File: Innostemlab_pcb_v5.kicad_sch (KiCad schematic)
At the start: 32 parts, among them J10 I2C, J11 ICSP, J2 USB4105-GF-A-060, J3 BATTERY, J4 MOTOR_1, J5 MOTOR_2, J6 IR1, J7 IR2, J8 IR3, J9 Conn_02x12_Odd_Even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

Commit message: Added caps in TB motor driver, added 22 ohm resistors in usb c data lines, changed part number for AVCC low pass filter, LD1117 datasheet from digikey shows same implementation
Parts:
- added C1, C2: 0.1uf, Capacitor_SMD:C_0805_2012Metric_Pad1.18x1.45mm_HandSolder, symbol Device:C
- added R4, R6: 22, Resistor_SMD:R_0805_2012Metric_Pad1.20x1.40mm_HandSolder, symbol Device:R
- L1: url digikey https://www.digikey.com/en/products/detail/kemet/L0805C100M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 -> https://www.digikey.com/en/products/detail/bourns-inc/MH202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
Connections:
- net +5V: now also C2.2
- net D+: now also R4.1; no longer U5.4 (D+)
- net D-: now also R6.1; no longer U5.3 (D-)
- net GND: now also C1.1, C2.1
- net VBATP_MD: now also C1.2
- new net DNET+: R4.2, U5.4 (D+)
- new net DNET-: R6.2, U5.3 (D-)
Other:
- moved on the sheet: AREF2

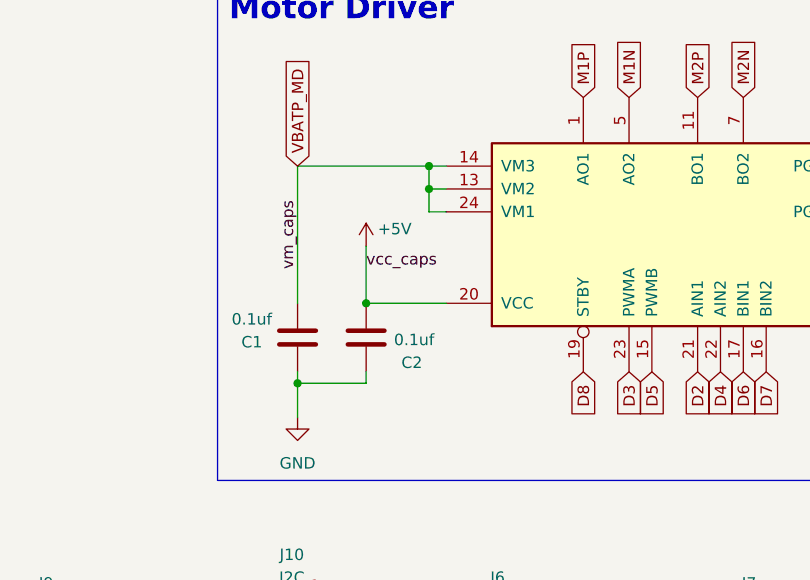
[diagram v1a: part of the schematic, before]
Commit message: Added electrolytic cap, changed motor nammmes to left and right
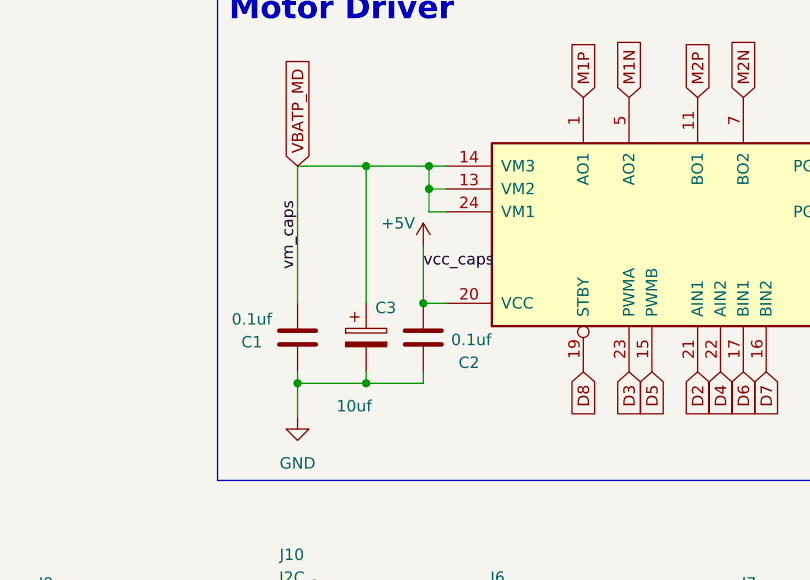
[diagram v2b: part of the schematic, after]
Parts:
- added C3: 10uf, Capacitor_Tantalum_SMD:CP_EIA-3528-12_Kemet-T, symbol Device:C_Polarized
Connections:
- net GND: now also C3.2
- net VBATP_MD: now also C3.1
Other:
- moved on the sheet: C2
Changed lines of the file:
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@@
 	)
 	(junction
+		(at 187.96 132.08)
+		(diameter 0)
+		(color 0 0 0 0)
+	)
+	(junction
 		(at 78.74 172.72)
 		(diameter 0)
@@
 	)
 	(junction
-		(at 187.96 123.19)
+		(at 194.31 123.19)
+		(diameter 0)
+		(color 0 0 0 0)
+	)
+	(junction
+		(at 187.96 107.95)
 		(diameter 0)
 		(color 0 0 0 0)
@@
 	(wire
 		(pts
+			(xy 194.31 116.84) (xy 194.31 123.19)
+		)
+		(stroke
+			(width 0)
+			(type default)
+		)
+	)
+	(wire
+		(pts
 			(xy 240.03 59.055) (xy 251.46 59.055)
 		)
@@
 	(wire
 		(pts
+			(xy 187.96 132.08) (xy 194.31 132.08)
+		)
+		(stroke
+			(width 0)
+			(type default)
+		)
+	)
+	(wire
+		(pts
 			(xy 92.71 40.64) (xy 96.52 40.64)
 		)
@@
 	(wire
 		(pts
-			(xy 180.34 107.95) (xy 194.945 107.95)
+			(xy 180.34 107.95) (xy 187.96 107.95)
 		)
 		(stroke
@@
 	(wire
 		(pts
+			(xy 187.96 107.95) (xy 194.945 107.95)
+		)
+		(stroke
+			(width 0)
+			(type default)
+		)
+	)
+	(wire
+		(pts
 			(xy 180.34 132.08) (xy 187.96 132.08)
 		)
@@
 	(wire
 		(pts
-			(xy 187.96 123.19) (xy 196.85 123.19)
+			(xy 194.31 123.19) (xy 196.85 123.19)
 		)
 		(stroke
@@
 	(wire
 		(pts
+			(xy 187.96 130.81) (xy 187.96 132.08)
+		)
+		(stroke
+			(width 0)
+			(type default)
+		)
+	)
+	(wire
+		(pts
 			(xy 210.82 68.58) (xy 220.98 68.58)
 		)
@@
 	(wire
 		(pts
-			(xy 187.96 116.84) (xy 187.96 123.19)
-		)
-		(stroke
-			(width 0)
-			(type default)
-		)
-	)
-	(wire
-		(pts
 			(xy 41.91 71.12) (xy 44.45 71.12)
 		)
@@
 	(wire
 		(pts
-			(xy 187.96 132.08) (xy 187.96 130.81)
+			(xy 194.31 132.08) (xy 194.31 130.81)
+		)
+		(stroke
+			(width 0)
+			(type default)
+		)
+	)
+	(wire
+		(pts
+			(xy 187.96 107.95) (xy 187.96 123.19)
 		)
 		(stroke
@@
 	)
 	(label "vcc_caps"
-		(at 187.96 119.38 0)
+		(at 194.31 119.38 0)
 		(effects
 			(font
@@
 	(symbol
 		(lib_id "power:+5V")
-		(at 187.96 116.84 0)
+		(at 194.31 116.84 0)
 		(unit 1)
 		(exclude_from_sim no)
@@
 		(dnp no)
 		(property "Reference" "#PWR027"
-			(at 187.96 120.65 0)
+			(at 194.31 120.65 0)
 			(effects
 				(font
@@
 		)
 		(property "Value" "+5V"
-			(at 191.135 114.935 0)
+			(at 191.516 114.3 0)
 			(effects
 				(font
@@
 		)
 		(property "Footprint" ""
-			(at 187.96 116.84 0)
+			(at 194.31 116.84 0)
 			(effects
 				(font
@@
 		)
 		(property "Datasheet" ""
-			(at 187.96 116.84 0)
+			(at 194.31 116.84 0)
 			(effects
 				(font
@@
 		)
 		(property "Description" ""
-			(at 187.96 116.84 0)
+			(at 194.31 116.84 0)
 			(effects
 				(font
@@
 	)
 	(symbol
+		(lib_id "Device:C_Polarized")
+		(at 187.96 127 0)
+		(unit 1)
+		(exclude_from_sim no)
+		(in_bom yes)
+		(on_board yes)
+		(dnp no)
+		(property "Reference" "C3"
+			(at 188.976 123.698 0)
+			(effects
+				(font
+					(size 1.27 1.27)
+				)
+				(justify left)
+			)
+		)
+		(property "Value" "10uf"
+			(at 184.658 134.62 0)
+			(effects
+				(font
+					(size 1.27 1.27)
+				)
+				(justify left)
+			)
+		)
+		(property "Footprint" "Capacitor_Tantalum_SMD:CP_EIA-3528-12_Kemet-T"
+			(at 188.9252 130.81 0)
+			(effects
+				(font
+					(size 1.27 1.27)
+				)
+				(hide yes)
+			)
+		)
+		(property "Datasheet" "https://www.digikey.com/en/products/detail/cal-chip-electronics-inc/TCMIC106BT/22168875?gclsrc=aw.ds&gad_source=1&gad_campaignid=20228387720&gbraid=0AAAAADrbLlhYw3Z1zR07cKJtpWXjwg5ZN&gclid=CjwKCAjwxrLHBhA2EiwAu9EdM1dvaXxue4vfuhmBPfpXiSDI0lTKTG98ig32ygW_xHK9Nhn3t-lPchoCIDgQAvD_BwE"
+			(at 187.96 127 0)
+			(effects
+				(font
+					(size 1.27 1.27)
+				)
+				(hide yes)
+			)
+		)
+		(property "Description" "Polarized capacitor"
+			(at 187.96 127 0)
+			(effects
+				(font
+					(size 1.27 1.27)
+				)
+				(hide yes)
+			)
+		)
+		(pin "1"
+		)
+		(pin "2"
+		)
+		(instances
+			(project ""
+				(path "/f5107db4-43c3-49e1-b053-f3fcbaac6752"
+					(reference "C3")
+					(unit 1)
+				)
+			)
+		)
+	)
+	(symbol
 		(lib_id "Connector_Generic:Conn_02x03_Odd_Even")
 		(at 40.64 123.19 0)
@@
 	(symbol
 		(lib_id "Device:C")
-		(at 187.96 127 180)
+		(at 194.31 127 180)
 		(unit 1)
 		(exclude_from_sim no)
@@
 		(dnp no)
 		(property "Reference" "C2"
-			(at 193.04 129.794 0)
+			(at 199.39 129.794 0)
 			(effects
 				(font
@@
 		)
 		(property "Value" "0.1uf"
-			(at 193.294 127.254 0)
+			(at 199.644 127.254 0)
 			(effects
 				(font
@@
 		)
 		(property "Footprint" "Capacitor_SMD:C_0805_2012Metric_Pad1.18x1.45mm_HandSolder"
-			(at 186.9948 123.19 0)
+			(at 193.3448 123.19 0)
 			(effects
 				(font
@@
 		)
 		(property "Datasheet" "~"
-			(at 187.96 127 0)
+			(at 194.31 127 0)
 			(effects
 				(font
@@
 		)
 		(property "Description" ""
-			(at 187.96 127 0)
+			(at 194.31 127 0)
 			(effects
 				(font

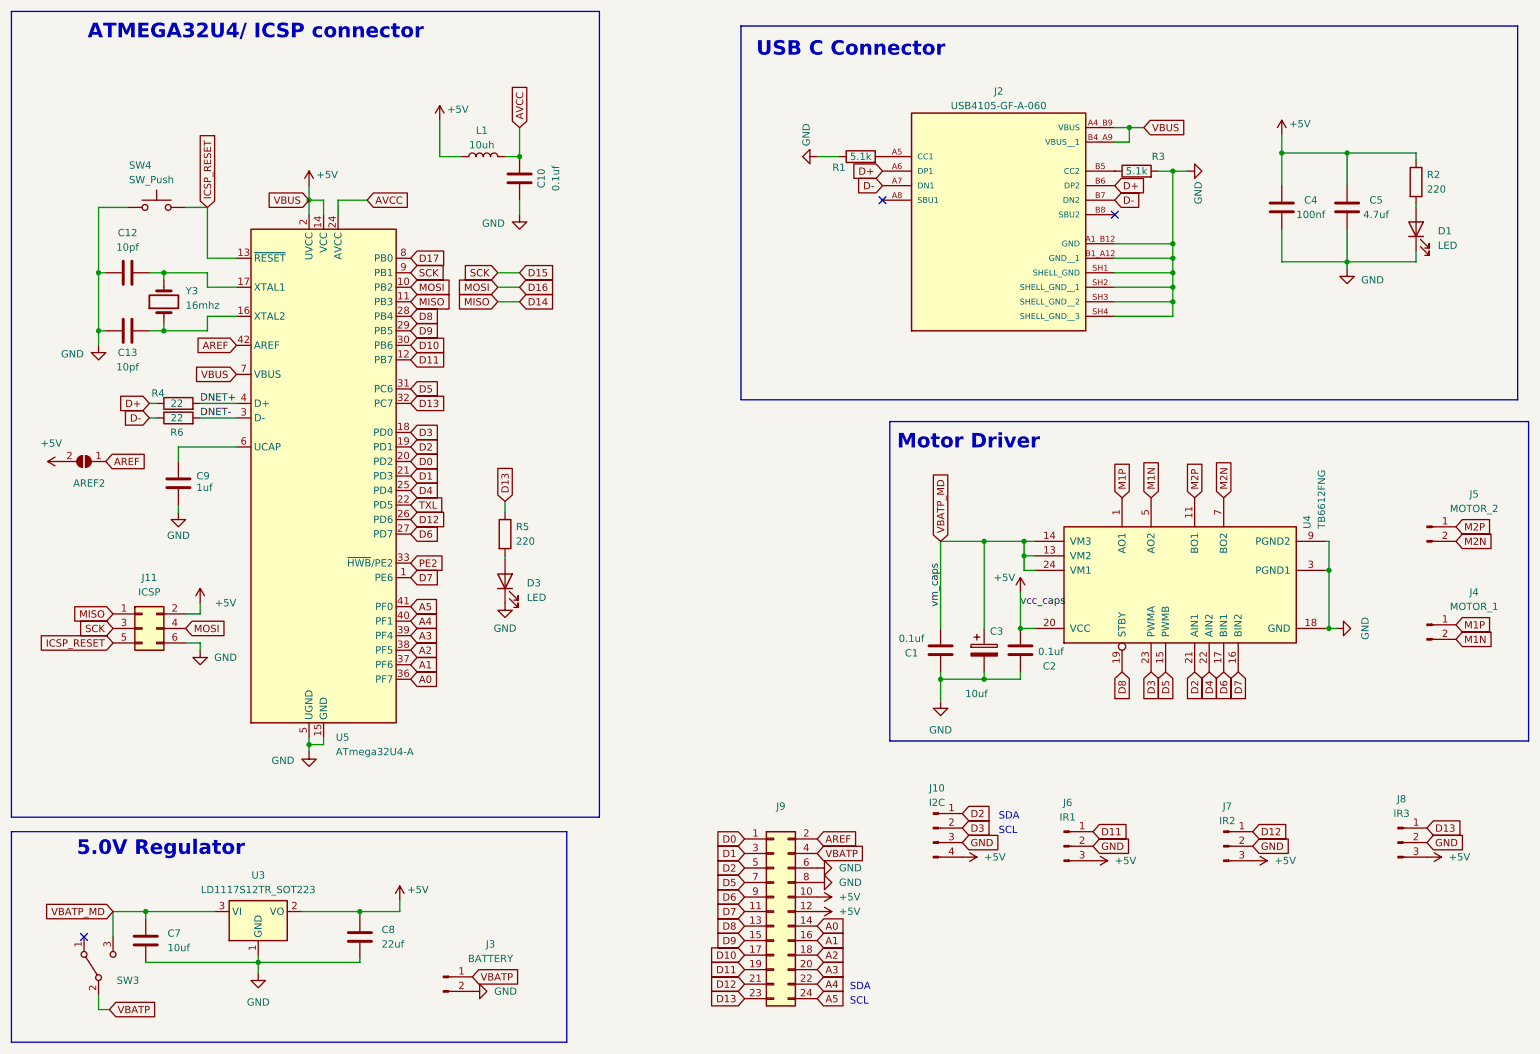
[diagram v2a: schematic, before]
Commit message: updated vbus and 5v to be seperate so that usb only powers atmega chip. battery required for other sensors and components
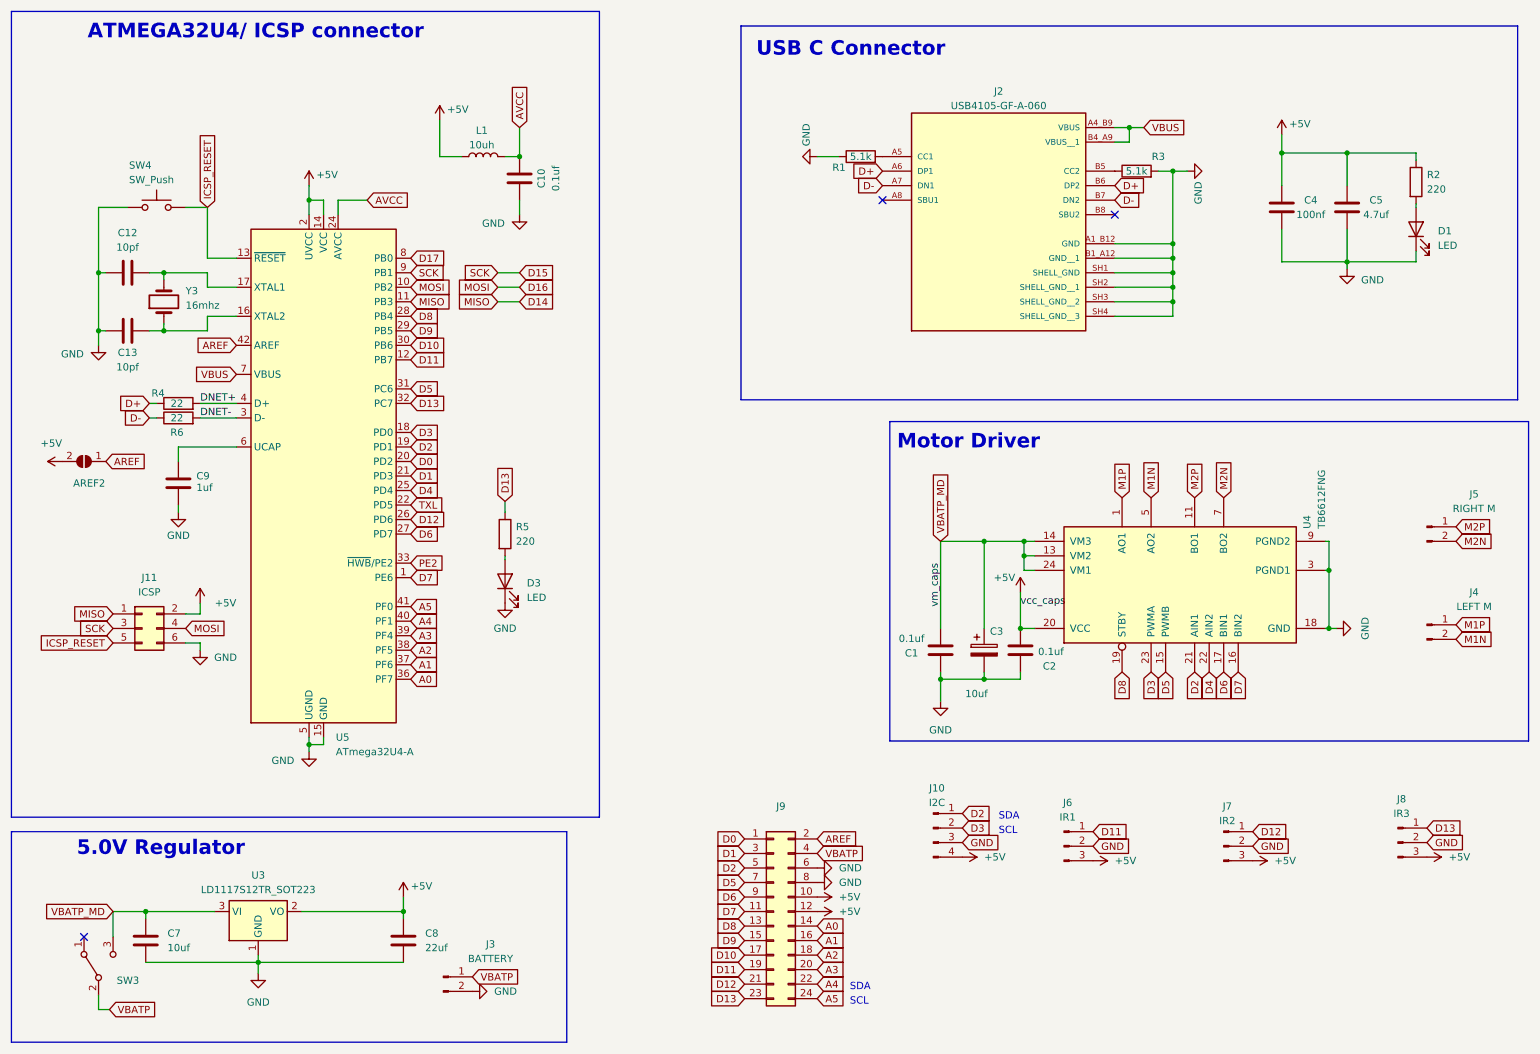
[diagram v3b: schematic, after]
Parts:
- J4: value MOTOR_1 -> LEFT M
- J5: value MOTOR_2 -> RIGHT M
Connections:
- net +5V: no longer J2.A4_B9 (VBUS), J2.B4_A9 (VBUS__1), U5.7 (VBUS)
- new net VBUS: J2.A4_B9 (VBUS), J2.B4_A9 (VBUS__1), U5.7 (VBUS)
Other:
- moved on the sheet: C8
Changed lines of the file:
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@@
 	)
 	(junction
+		(at 86.36 172.72)
+		(diameter 0)
+		(color 0 0 0 0)
+	)
+	(junction
 		(at 33.02 60.96)
 		(diameter 0)
@@
 	)
 	(junction
-		(at 78.74 172.72)
-		(diameter 0)
-		(color 0 0 0 0)
-	)
-	(junction
 		(at 220.98 43.18)
 		(diameter 0)
@@
 	(wire
 		(pts
-			(xy 78.74 173.355) (xy 78.74 172.72)
+			(xy 86.36 173.99) (xy 86.36 172.72)
 		)
 		(stroke
@@
 	(wire
 		(pts
-			(xy 78.74 181.61) (xy 60.96 181.61)
+			(xy 86.36 181.61) (xy 60.96 181.61)
 		)
 		(stroke
@@
 	(wire
 		(pts
-			(xy 78.74 172.72) (xy 68.58 172.72)
+			(xy 68.58 172.72) (xy 86.36 172.72)
 		)
 		(stroke
@@
 	(wire
 		(pts
-			(xy 85.725 172.72) (xy 78.74 172.72)
-		)
-		(stroke
-			(width 0)
-			(type default)
-		)
-	)
-	(wire
-		(pts
 			(xy 33.02 187.325) (xy 33.02 189.865)
 		)
@@
 	(wire
 		(pts
-			(xy 85.725 170.815) (xy 85.725 172.72)
-		)
-		(stroke
-			(width 0)
-			(type default)
-		)
-	)
-	(wire
-		(pts
-			(xy 78.74 181.61) (xy 78.74 180.975)
+			(xy 86.36 170.18) (xy 86.36 172.72)
 		)
 		(stroke
@@
 		)
 	)
-	(global_label "VBUS"
-		(shape input)
-		(at 69.85 48.26 180)
-		(fields_autoplaced yes)
-		(effects
-			(font
-				(size 1.27 1.27)
-			)
-			(justify right)
-		)
-		(property "Intersheetrefs" "${INTERSHEET_REFS}"
-			(at 61.9662 48.26 0)
-			(effects
-				(font
-					(size 1.27 1.27)
-				)
-				(justify right)
-				(hide yes)
-			)
-		)
-	)
 	(global_label "D14"
 		(shape input)
@@
 	(symbol
 		(lib_id "power:+5V")
-		(at 85.725 170.815 0)
+		(at 86.36 170.18 0)
 		(unit 1)
 		(exclude_from_sim no)
@@
 		(dnp no)
 		(property "Reference" "#PWR013"
-			(at 85.725 174.625 0)
+			(at 86.36 173.99 0)
 			(effects
 				(font
@@
 		)
 		(property "Value" "+5V"
-			(at 88.9 168.91 0)
+			(at 89.535 168.275 0)
 			(effects
 				(font
@@
 		)
 		(property "Footprint" ""
-			(at 85.725 170.815 0)
+			(at 86.36 170.18 0)
 			(effects
 				(font
@@
 		)
 		(property "Datasheet" ""
-			(at 85.725 170.815 0)
+			(at 86.36 170.18 0)
 			(effects
 				(font
@@
 		)
 		(property "Description" ""
-			(at 85.725 170.815 0)
+			(at 86.36 170.18 0)
 			(effects
 				(font
@@
 	(symbol
 		(lib_id "Device:C")
-		(at 78.74 177.165 0)
+		(at 86.36 177.8 0)
 		(unit 1)
 		(exclude_from_sim no)
@@
 		(fields_autoplaced yes)
 		(property "Reference" "C8"
-			(at 82.55 175.895 0)
+			(at 90.17 176.53 0)
 			(effects
 				(font
@@
 		)
 		(property "Value" "22uf"
-			(at 82.55 178.435 0)
+			(at 90.17 179.07 0)
 			(effects
 				(font
@@
 		)
 		(property "Footprint" "Capacitor_SMD:C_0805_2012Metric_Pad1.18x1.45mm_HandSolder"
-			(at 79.7052 180.975 0)
+			(at 87.3252 181.61 0)
 			(effects
 				(font
@@
 		)
 		(property "Datasheet" "~"
-			(at 78.74 177.165 0)
+			(at 86.36 177.8 0)
 			(effects
 				(font
@@
 		)
 		(property "Description" ""
-			(at 78.74 177.165 0)
+			(at 86.36 177.8 0)
 			(effects
 				(font
@@
 			)
 		)
-		(property "Value" "MOTOR_1"
+		(property "Value" "LEFT M"
 			(at 273.685 119.38 0)
 			(effects
@@
 			)
 		)
-		(property "Value" "MOTOR_2"
+		(property "Value" "RIGHT M"
 			(at 273.685 102.235 0)
 			(effects
